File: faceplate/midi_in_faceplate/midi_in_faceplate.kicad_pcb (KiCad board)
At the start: 2 copper layers, 98 x 30 mm, 3 parts

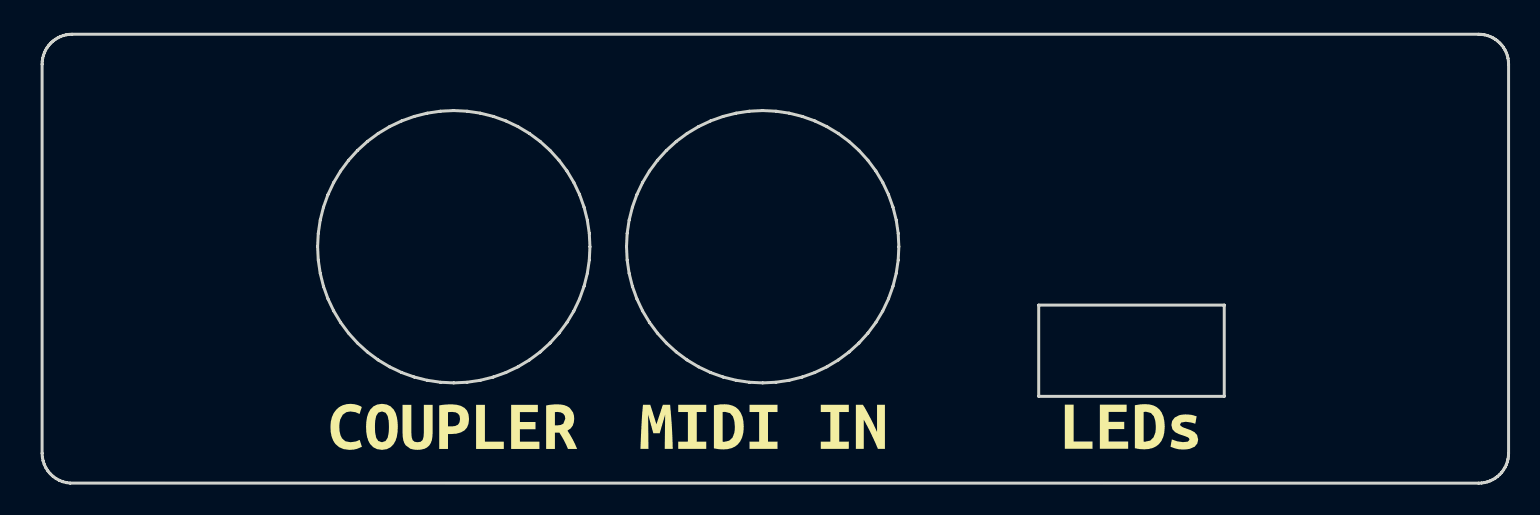
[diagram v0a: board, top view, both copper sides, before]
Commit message: Tweak MIDI ports to match PCB
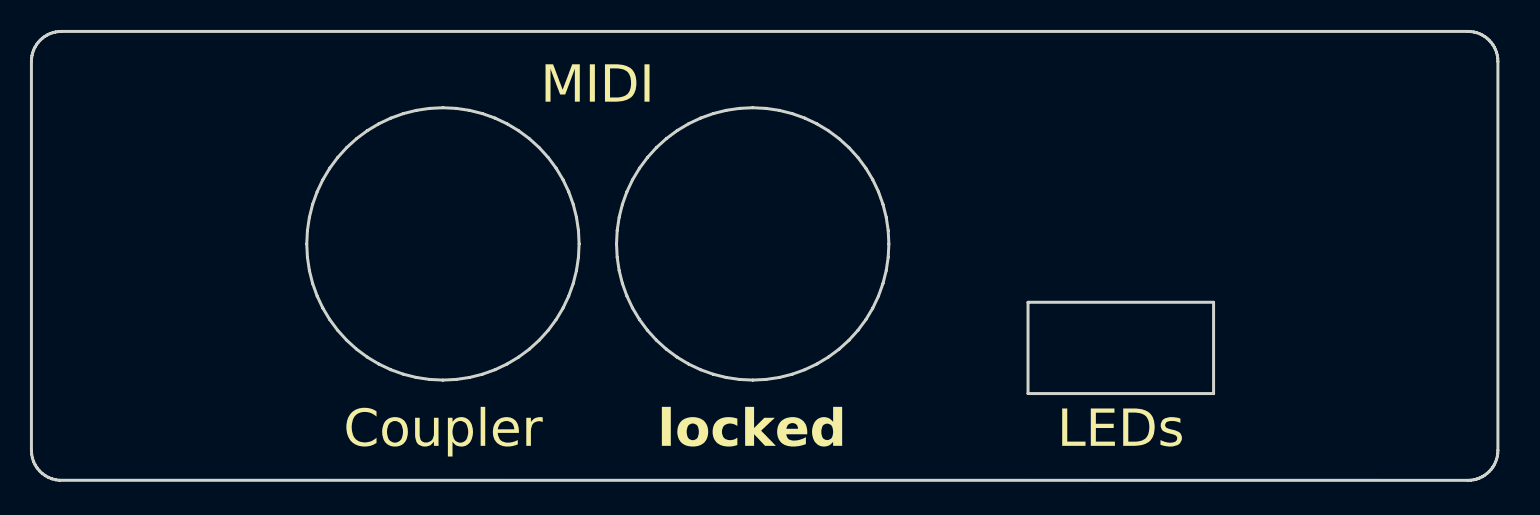
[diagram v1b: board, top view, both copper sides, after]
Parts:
- removed kibuzzard-64094DD9: G***, kibuzzard-64094DD9
- removed kibuzzard-64094E0D: G***, kibuzzard-64094E0D
- removed kibuzzard-64094E55: G***, kibuzzard-64094E55
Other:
- outline, holes or cut-outs redrawn
- board text added: "Coupler"
- board text added: "LEDs"
- board text added: "MIDI"
- board text added: "locked"
